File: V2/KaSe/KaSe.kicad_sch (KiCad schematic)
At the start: 158 parts, among them J1 gc9a01_DISPLAY, J2 Conn_01x06, J4 Conn_01x03, J5 Conn_01x03, Q1 BSS83P, Q2 BSS83P, SW1 SWITCH_PUSH, SW10 SWITCH_PUSH, SW11 SWITCH_PUSH, SW12 SWITCH_PUSH, SW13 SWITCH_PUSH, SW14 SWITCH_PUSH, SW15 SWITCH_PUSH, SW16 SWITCH_PUSH, SW17 SWITCH_PUSH, SW18 SWITCH_PUSH, SW19 SWITCH_PUSH, SW2 SWITCH_PUSH, SW20 SWITCH_PUSH, SW21 SWITCH_PUSH, SW22 SWITCH_PUSH, SW23 SWITCH_PUSH, SW24 SWITCH_PUSH, SW25 SWITCH_PUSH, SW26 SWITCH_PUSH, SW27 SWITCH_PUSH, SW28 SWITCH_PUSH, SW29 SWITCH_PUSH, SW3 SWITCH_PUSH, SW30 SWITCH_PUSH, SW31 SWITCH_PUSH, SW32 SWITCH_PUSH, SW33 SWITCH_PUSH, SW34 SWITCH_PUSH, SW36 SWITCH_PUSH, SW37 SWITCH_PUSH, SW38 SWITCH_PUSH, SW39 SWITCH_PUSH, SW4 SWITCH_PUSH, SW40 SWITCH_PUSH, SW41 SWITCH_PUSH, SW42 SWITCH_PUSH, SW43 SWITCH_PUSH, SW44 SWITCH_PUSH, SW45 SWITCH_PUSH, SW46 SWITCH_PUSH, SW47 SWITCH_PUSH, SW48 SWITCH_PUSH, SW49 SWITCH_PUSH, SW5 SWITCH_PUSH, SW50 SWITCH_PUSH, SW51 SWITCH_PUSH, SW52 SWITCH_PUSH, SW53 SWITCH_PUSH, SW54 SWITCH_PUSH, SW55 SWITCH_PUSH, SW56 SWITCH_PUSH, SW57 SWITCH_PUSH, SW58 SWITCH_PUSH, SW59 SWITCH_PUSH, SW6 SWITCH_PUSH, SW60 SWITCH_PUSH, SW61 SWITCH_PUSH, SW62 SWITCH_PUSH, SW63 SWITCH_PUSH, SW64 SWITCH_PUSH, SW65 SWITCH_PUSH, SW7 SWITCH_PUSH, SW8 SWITCH_PUSH, SW9 SWITCH_PUSH, U1 NRF24L01_Breakout, U2 AP130-33SA, U3 ESP32-S3-DevKitC, U4 TLV73333PDBV

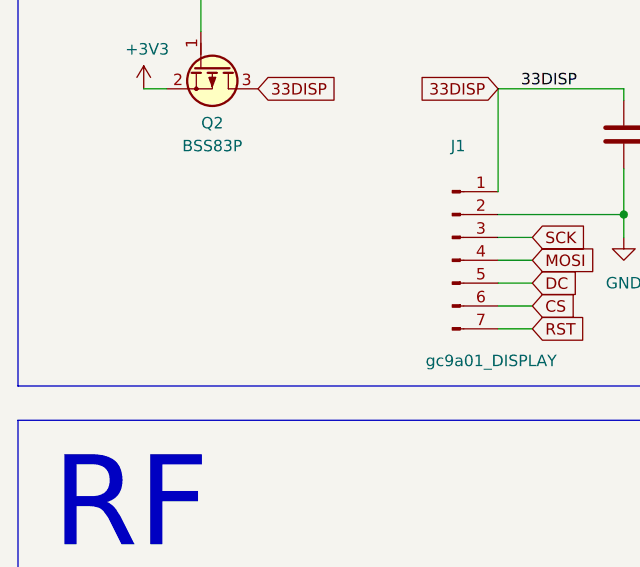
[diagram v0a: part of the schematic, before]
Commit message: add i2c display ssd1306 and clean up for print
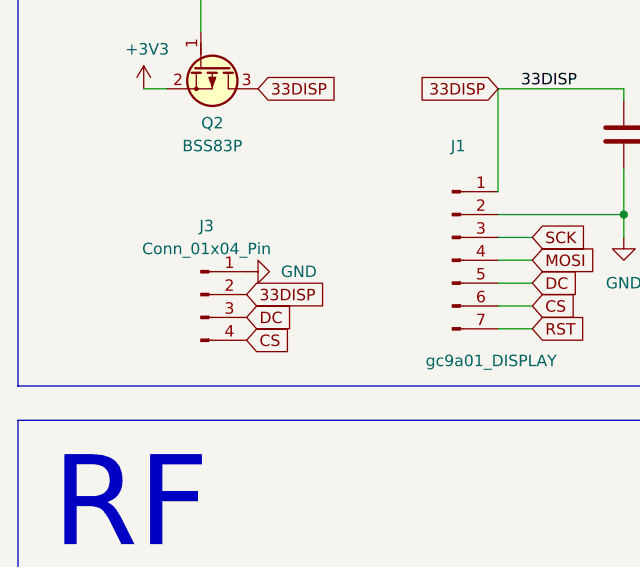
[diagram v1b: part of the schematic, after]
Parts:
- added J3: Conn_01x04_Pin, Connector_PinHeader_2.54mm:PinHeader_1x04_P2.54mm_Vertical, symbol Connector:Conn_01x04_Pin
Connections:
- net 33DISP: now also J3.2 (Pin_2)
- net CS: now also J3.4 (Pin_4)
- net DC: now also J3.3 (Pin_3)
- net GND: now also J3.1 (Pin_1)
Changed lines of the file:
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@@
 		)
 	)
+	(global_label "33DISP"
+		(shape input)
+		(at 45.72 300.99 0)
+		(fields_autoplaced yes)
+		(effects
+			(font
+				(size 1.27 1.27)
+			)
+			(justify left)
+		)
+		(property "Intersheetrefs" "${INTERSHEET_REFS}"
+			(at 54.8243 300.99 0)
+			(effects
+				(font
+					(size 1.27 1.27)
+				)
+				(justify left)
+				(hide yes)
+			)
+		)
+	)
 	(global_label "ALIM_NRF"
 		(shape input)
@@
 	(global_label "DC"
 		(shape input)
+		(at 45.72 303.53 0)
+		(fields_autoplaced yes)
+		(effects
+			(font
+				(size 1.27 1.27)
+			)
+			(justify left)
+		)
+		(property "Intersheetrefs" "${INTERSHEET_REFS}"
+			(at 50.591 303.53 0)
+			(effects
+				(font
+					(size 1.27 1.27)
+				)
+				(justify left)
+				(hide yes)
+			)
+		)
+	)
+	(global_label "DC"
+		(shape input)
 		(at 488.95 99.06 0)
 		(fields_autoplaced yes)
@@
 		)
 	)
+	(global_label "CS"
+		(shape input)
+		(at 45.72 306.07 0)
+		(fields_autoplaced yes)
+		(effects
+			(font
+				(size 1.27 1.27)
+			)
+			(justify left)
+		)
+		(property "Intersheetrefs" "${INTERSHEET_REFS}"
+			(at 50.5305 306.07 0)
+			(effects
+				(font
+					(size 1.27 1.27)
+				)
+				(justify left)
+				(hide yes)
+			)
+		)
+	)
 	(global_label "B-"
 		(shape input)
@@
 					(unit 1)
 				)
+			)
+		)
+	)
+	(symbol
+		(lib_id "power:GND")
+		(at 45.72 298.45 90)
+		(unit 1)
+		(exclude_from_sim no)
+		(in_bom yes)
+		(on_board yes)
+		(dnp no)
+		(fields_autoplaced yes)
+		(property "Reference" "#PWR02"
+			(at 52.07 298.45 0)
+			(effects
+				(font
+					(size 1.27 1.27)
+				)
+				(hide yes)
+			)
+		)
+		(property "Value" "GND"
+			(at 49.53 298.4499 90)
+			(effects
+				(font
+					(size 1.27 1.27)
+				)
+				(justify right)
+			)
+		)
+		(property "Footprint" ""
+			(at 45.72 298.45 0)
+			(effects
+				(font
+					(size 1.27 1.27)
+				)
+				(hide yes)
+			)
+		)
+		(property "Datasheet" ""
+			(at 45.72 298.45 0)
+			(effects
+				(font
+					(size 1.27 1.27)
+				)
+				(hide yes)
+			)
+		)
+		(property "Description" ""
+			(at 45.72 298.45 0)
+			(effects
+				(font
+					(size 1.27 1.27)
+				)
+				(hide yes)
+			)
+		)
+		(pin "1"
+		)
+		(instances
+			(project "KaSe"
+				(path "/aeb6a6d4-f0d5-44e2-86f8-9901b2370183"
+					(reference "#PWR02")
+					(unit 1)
+				)
+			)
+		)
+	)
+	(symbol
+		(lib_id "Connector:Conn_01x04_Pin")
+		(at 40.64 300.99 0)
+		(unit 1)
+		(exclude_from_sim no)
+		(in_bom yes)
+		(on_board yes)
+		(dnp no)
+		(fields_autoplaced yes)
+		(property "Reference" "J3"
+			(at 41.275 293.37 0)
+			(effects
+				(font
+					(size 1.27 1.27)
+				)
+			)
+		)
+		(property "Value" "Conn_01x04_Pin"
+			(at 41.275 295.91 0)
+			(effects
+				(font
+					(size 1.27 1.27)
+				)
+			)
+		)
+		(property "Footprint" "Connector_PinHeader_2.54mm:PinHeader_1x04_P2.54mm_Vertical"
+			(at 40.64 300.99 0)
+			(effects
+				(font
+					(size 1.27 1.27)
+				)
+				(hide yes)
+			)
+		)
+		(property "Datasheet" "~"
+			(at 40.64 300.99 0)
+			(effects
+				(font
+					(size 1.27 1.27)
+				)
+				(hide yes)
+			)
+		)
+		(property "Description" "Generic connector, single row, 01x04, script generated"
+			(at 40.64 300.99 0)
+			(effects
+				(font
+					(size 1.27 1.27)
+				)
+				(hide yes)
+			)
+		)
+		(pin "2"
+		)
+		(pin "1"
+		)
+		(pin "3"
+		)
+		(pin "4"
+		)
+		(instances
+			(project ""
+				(path "/aeb6a6d4-f0d5-44e2-86f8-9901b2370183"
+					(reference "J3")
+					(unit 1)
+				)

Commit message: e
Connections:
- net COL7: now also U3.27 (GPIO21); no longer U3.43 (GPIO43/U0TXD)
- net COL8: now also U3.34 (GPIO37); no longer U3.42 (GPIO44/U0RXD)
- net LED_WS: no longer U3.27 (GPIO21)
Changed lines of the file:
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@@
 	(wire
 		(pts
-			(xy 488.95 124.46) (xy 481.33 124.46)
-		)
-		(stroke
-			(width 0)
-			(type default)
-		)
-	)
-	(wire
-		(pts
 			(xy 335.28 130.81) (xy 335.28 125.73)
 		)
@@
 	(wire
 		(pts
+			(xy 508 132.08) (xy 481.33 132.08)
+		)
+		(stroke
+			(width 0)
+			(type default)
+		)
+	)
+	(wire
+		(pts
 			(xy 488.95 91.44) (xy 481.33 91.44)
 		)
@@
 	(wire
 		(pts
+			(xy 481.33 124.46) (xy 508 124.46)
+		)
+		(stroke
+			(width 0)
+			(type default)
+		)
+	)
+	(wire
+		(pts
 			(xy 86.36 77.47) (xy 86.36 85.09)
 		)
@@
 		)
 	)
+	(global_label "COL8"
+		(shape input)
+		(at 502.92 66.04 0)
+		(fields_autoplaced yes)
+		(effects
+			(font
+				(size 1.27 1.27)
+			)
+			(justify left)
+		)
+		(property "Intersheetrefs" "${INTERSHEET_REFS}"
+			(at 510.0891 66.04 0)
+			(effects
+				(font
+					(size 1.27 1.27)
+				)
+				(justify left)
+				(hide yes)
+			)
+		)
+	)
 	(global_label "ALIM_DISP"
 		(shape input)
@@
 		)
 	)
+	(global_label "COL7"
+		(shape input)
+		(at 502.92 63.5 0)
+		(fields_autoplaced yes)
+		(effects
+			(font
+				(size 1.27 1.27)
+			)
+			(justify left)
+		)
+		(property "Intersheetrefs" "${INTERSHEET_REFS}"
+			(at 510.0891 63.5 0)
+			(effects
+				(font
+					(size 1.27 1.27)
+				)
+				(justify left)
+				(hide yes)
+			)
+		)
+	)
 	(global_label "OUT+"
 		(shape input)
@@
 	(global_label "COL8"
 		(shape input)
-		(at 481.33 66.04 0)
+		(at 508 132.08 0)
 		(fields_autoplaced yes)
 		(effects
@@
 		)
 		(property "Intersheetrefs" "${INTERSHEET_REFS}"
-			(at 488.4991 66.04 0)
+			(at 515.1691 132.08 0)
 			(effects
 				(font
@@
 	(global_label "LED_WS"
 		(shape input)
-		(at 488.95 124.46 0)
+		(at 513.08 111.76 0)
 		(fields_autoplaced yes)
 		(effects
@@
 		)
 		(property "Intersheetrefs" "${INTERSHEET_REFS}"
-			(at 498.3566 124.46 0)
+			(at 522.4866 111.76 0)
 			(effects
 				(font
@@
 	(global_label "COL7"
 		(shape input)
-		(at 481.33 63.5 0)
+		(at 508 124.46 0)
 		(fields_autoplaced yes)
 		(effects
@@
 		)
 		(property "Intersheetrefs" "${INTERSHEET_REFS}"
-			(at 488.4991 63.5 0)
+			(at 515.1691 124.46 0)
 			(effects
 				(font
